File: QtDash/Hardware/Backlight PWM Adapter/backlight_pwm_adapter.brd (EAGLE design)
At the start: 40.4 x 19.5 mm, 12 parts, among them Q1 310mA/60V/1.6Ω, Q2 310mA/60V/1.6Ω

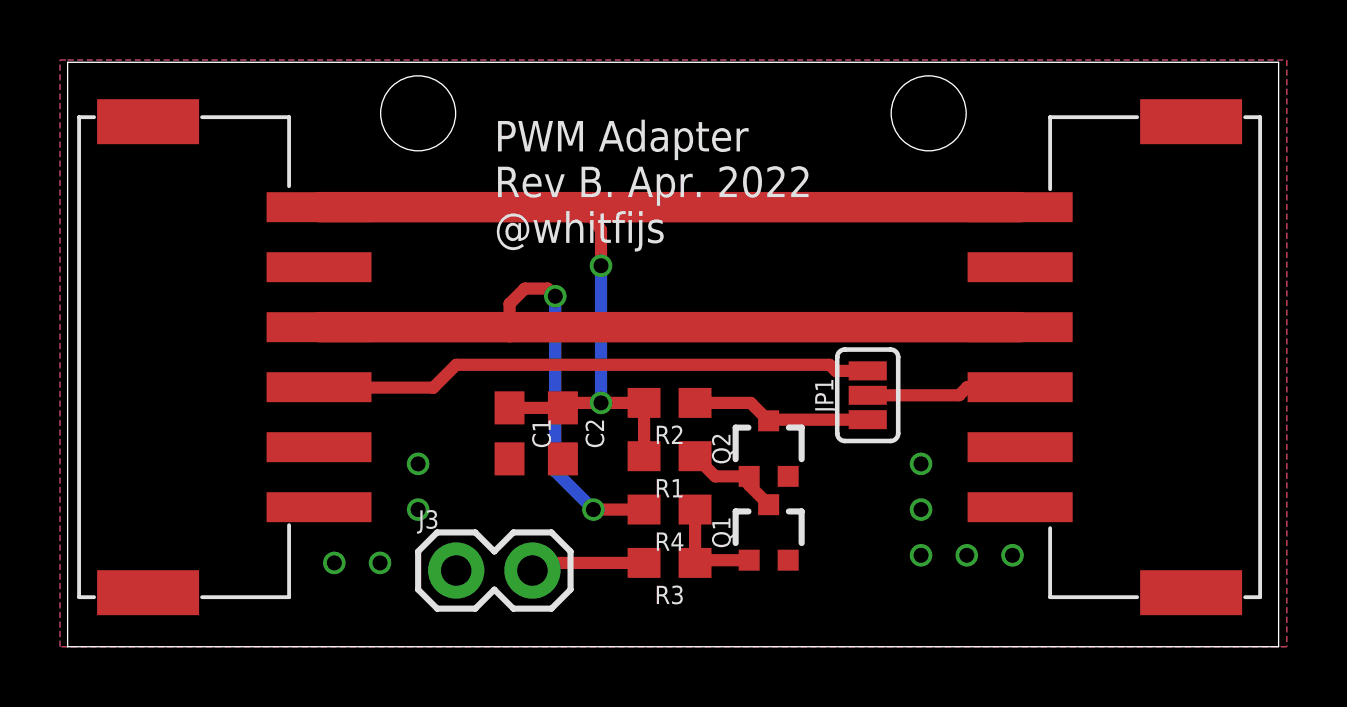
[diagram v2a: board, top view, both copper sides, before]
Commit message: topic/hardware-revc: 	- open drain for PWM adapter made non-inverting -- keeps backlight on during boot 	- made use of activeLow backlight config 	- changed backlight initialization values in inittab 	- changed config.ini active low to true
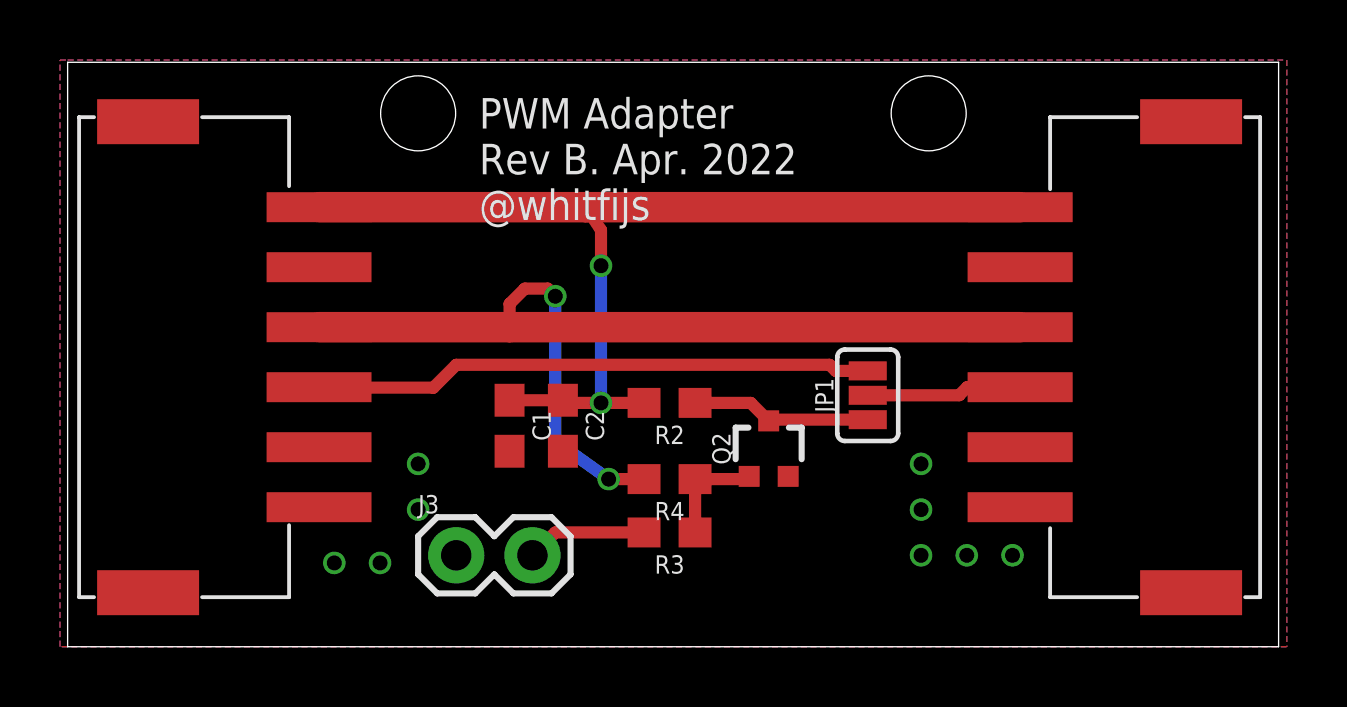
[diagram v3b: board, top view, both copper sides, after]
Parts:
- removed Q1: 310mA/60V/1.6Ω, SparkFun-DiscreteSemi:SOT323
- removed R1: 1k, digital_dash:0603
- moved R3 1.02 mm to (20.3, 3.81)
- moved R4 1.02 mm to (20.3, 5.59)
- moved J3 0.51 mm to (13.2, 3.05)
- moved C1 0.25 mm to (15.0, 7.37)
- moved C2 0.25 mm to (16.8, 7.37)
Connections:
- removed net N$3: Q1.3, Q2.1, R1.1
- net 5V: no longer R1.2
- net GND: no longer Q1.2
- net N$2: now also Q2.1; no longer Q1.1
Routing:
- net N$3: track 3.29 -> 0.00 mm
- net 5V: track 36.5 -> 34.6 mm
- net 3.3V: track 35.3 -> 34.2 mm
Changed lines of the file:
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@@
 <circle x="28.956" y="17.78" radius="1.27" width="0.4064" layer="42"/>
 <circle x="28.956" y="17.78" radius="1.27" width="0.4064" layer="41"/>
-<text x="14.478" y="13.462" size="1.016" layer="21" font="vector" ratio="15">PWM Adapter
+<text x="13.97" y="14.224" size="1.016" layer="21" font="vector" ratio="15">PWM Adapter
 Rev B. Apr. 2022
 @whitfijs</text>
@@
 <element name="J2" library="backlight_pwm_adapter" package="140-506-417-060" value="" x="32.004" y="9.652" rot="R270"/>
 <element name="JP1" library="SparkFun-Jumpers" package="SMT-JUMPER_3_NO_SILK" value="JUMPER-SMT_3_NO_SILK" x="26.924" y="8.382" rot="R90"/>
-<element name="Q1" library="SparkFun-DiscreteSemi" package="SOT323" value="310mA/60V/1.6Ω" x="23.622" y="3.81">
-<attribute name="PROD_ID" value="TRANS-11151" x="23.622" y="3.81" size="1.778" layer="27" display="off"/>
-</element>
 <element name="Q2" library="SparkFun-DiscreteSemi" package="SOT323" value="310mA/60V/1.6Ω" x="23.622" y="6.604">
 <attribute name="PROD_ID" value="TRANS-11151" x="23.622" y="6.604" size="1.778" layer="27" display="off"/>
 </element>
-<element name="R1" library="digital_dash" package="0603" value="1k" x="20.32" y="6.35" rot="R180"/>
 <element name="R2" library="digital_dash" package="0603" value="1k" x="20.32" y="8.128" rot="R180"/>
-<element name="J3" library="SparkFun-Connectors" package="1X02" value="" x="13.208" y="2.54"/>
-<element name="R3" library="digital_dash" package="0603" value="100R" x="20.32" y="2.794" rot="R180"/>
-<element name="C1" library="digital_dash" package="0603" value="100n" x="14.986" y="7.112" rot="R270">
-<attribute name="VOLTAGE" value="50V" x="14.986" y="7.112" size="1.778" layer="27" rot="R270" display="off"/>
+<element name="J3" library="SparkFun-Connectors" package="1X02" value="" x="13.208" y="3.048"/>
+<element name="R3" library="digital_dash" package="0603" value="100R" x="20.32" y="3.81" rot="R180"/>
+<element name="C1" library="digital_dash" package="0603" value="100n" x="14.986" y="7.366" rot="R270">
+<attribute name="VOLTAGE" value="50V" x="14.986" y="7.366" size="1.778" layer="27" rot="R270" display="off"/>
 </element>
-<element name="C2" library="digital_dash" package="0603" value="1u" x="16.764" y="7.112" rot="R270">
-<attribute name="VOLTAGE" value="25V" x="16.764" y="7.112" size="1.778" layer="27" rot="R270" display="off"/>
+<element name="C2" library="digital_dash" package="0603" value="1u" x="16.764" y="7.366" rot="R270">
+<attribute name="VOLTAGE" value="25V" x="16.764" y="7.366" size="1.778" layer="27" rot="R270" display="off"/>
 </element>
-<element name="R4" library="digital_dash" package="0603" value="20k" x="20.32" y="4.572" rot="R180"/>
+<element name="R4" library="digital_dash" package="0603" value="20k" x="20.32" y="5.588" rot="R180"/>
 </elements>
 <signals>
-<signal name="N$3">
-<contactref element="Q2" pad="1"/>
-<contactref element="R1" pad="1"/>
-<contactref element="Q1" pad="3"/>
-<wire x1="23.622" y1="4.735" x2="22.972" y2="5.385" width="0.4064" layer="1"/>
-<wire x1="22.972" y1="5.385" x2="22.972" y2="5.679" width="0.4064" layer="1"/>
-<wire x1="21.17" y1="6.35" x2="21.841" y2="5.679" width="0.4064" layer="1"/>
-<wire x1="21.841" y1="5.679" x2="22.972" y2="5.679" width="0.4064" layer="1"/>
-</signal>
 <signal name="GND">
-<contactref element="Q1" pad="2"/>
 <contactref element="Q2" pad="2"/>
 <contactref element="J2" pad="1"/>
@@
 </signal>
 <signal name="5V">
-<contactref element="R1" pad="2"/>
 <contactref element="R2" pad="2"/>
 <contactref element="J2" pad="6"/>
@@
 <contactref element="C1" pad="1"/>
 <wire x1="18.034" y1="8.128" x2="16.764" y2="8.128" width="0.4064" layer="1"/>
-<wire x1="16.764" y1="8.128" x2="16.764" y2="7.962" width="0.4064" layer="1"/>
-<wire x1="16.764" y1="7.962" x2="14.986" y2="7.962" width="0.4064" layer="1"/>
-<wire x1="19.47" y1="6.35" x2="19.47" y2="8.128" width="0.4064" layer="1"/>
+<wire x1="16.764" y1="8.128" x2="16.764" y2="8.216" width="0.4064" layer="1"/>
+<wire x1="16.764" y1="8.216" x2="14.986" y2="8.216" width="0.4064" layer="1"/>
 </signal>
 <signal name="3.3V">
@@
 <contactref element="R4" pad="2"/>
 <wire x1="14.986" y1="10.652" x2="32.004" y2="10.652" width="1.016" layer="1"/>
-<wire x1="19.47" y1="4.572" x2="17.78" y2="4.572" width="0.4064" layer="1"/>
-<via x="17.78" y="4.572" extent="1-16" drill="0.5"/>
-<wire x1="17.78" y1="4.572" x2="16.51" y2="5.842" width="0.4064" layer="16"/>
-<wire x1="16.51" y1="5.842" x2="16.51" y2="11.684" width="0.4064" layer="16"/>
+<wire x1="19.47" y1="5.588" x2="18.288" y2="5.588" width="0.4064" layer="1"/>
+<via x="18.288" y="5.588" extent="1-16" drill="0.5"/>
+<wire x1="18.288" y1="5.588" x2="16.51" y2="6.858" width="0.4064" layer="16"/>
+<wire x1="16.51" y1="6.858" x2="16.51" y2="11.684" width="0.4064" layer="16"/>
 <via x="16.51" y="11.684" extent="1-16" drill="0.5"/>
 <wire x1="16.51" y1="11.684" x2="16.256" y2="11.938" width="0.4064" layer="1"/>
@@
 <contactref element="J3" pad="2"/>
 <contactref element="R3" pad="2"/>
-<wire x1="15.748" y1="2.54" x2="16.002" y2="2.794" width="0.4064" layer="1"/>
-<wire x1="16.002" y1="2.794" x2="19.47" y2="2.794" width="0.4064" layer="1"/>
+<wire x1="15.748" y1="3.048" x2="16.51" y2="3.81" width="0.4064" layer="1"/>
+<wire x1="16.51" y1="3.81" x2="19.47" y2="3.81" width="0.4064" layer="1"/>
 </signal>
 <signal name="N$2">
-<contactref element="Q1" pad="1"/>
 <contactref element="R3" pad="1"/>
 <contactref element="R4" pad="1"/>
-<wire x1="21.17" y1="2.794" x2="21.261" y2="2.885" width="0.4064" layer="1"/>
-<wire x1="21.261" y1="2.885" x2="22.972" y2="2.885" width="0.4064" layer="1"/>
-<wire x1="21.261" y1="2.885" x2="21.17" y2="2.976" width="0.4064" layer="1"/>
-<wire x1="21.17" y1="2.976" x2="21.17" y2="4.572" width="0.4064" layer="1"/>
+<wire x1="21.17" y1="3.81" x2="21.261" y2="3.901" width="0.4064" layer="1"/>
+<wire x1="21.261" y1="3.901" x2="21.17" y2="3.992" width="0.4064" layer="1"/>
+<wire x1="21.17" y1="3.992" x2="21.17" y2="5.588" width="0.4064" layer="1"/>
+<contactref element="Q2" pad="1"/>
+<wire x1="21.17" y1="5.588" x2="22.972" y2="5.588" width="0.4064" layer="1"/>
+<wire x1="22.972" y1="5.588" x2="22.972" y2="5.679" width="0.4064" layer="1"/>
 </signal>
 </signals>
